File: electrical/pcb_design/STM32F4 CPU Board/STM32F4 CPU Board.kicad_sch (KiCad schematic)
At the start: 37 parts, among them J1 STLINK_STDC14, J2 STLINK_TagConnect_6, J3 Conn_01x15_Pin, J4 Conn_01x15_Pin, M1 M3, M2 M3, M3 M3, M4 M3, U1 STM32F405RGT6, U2 AMS1117-3.3, Y1 16MHz

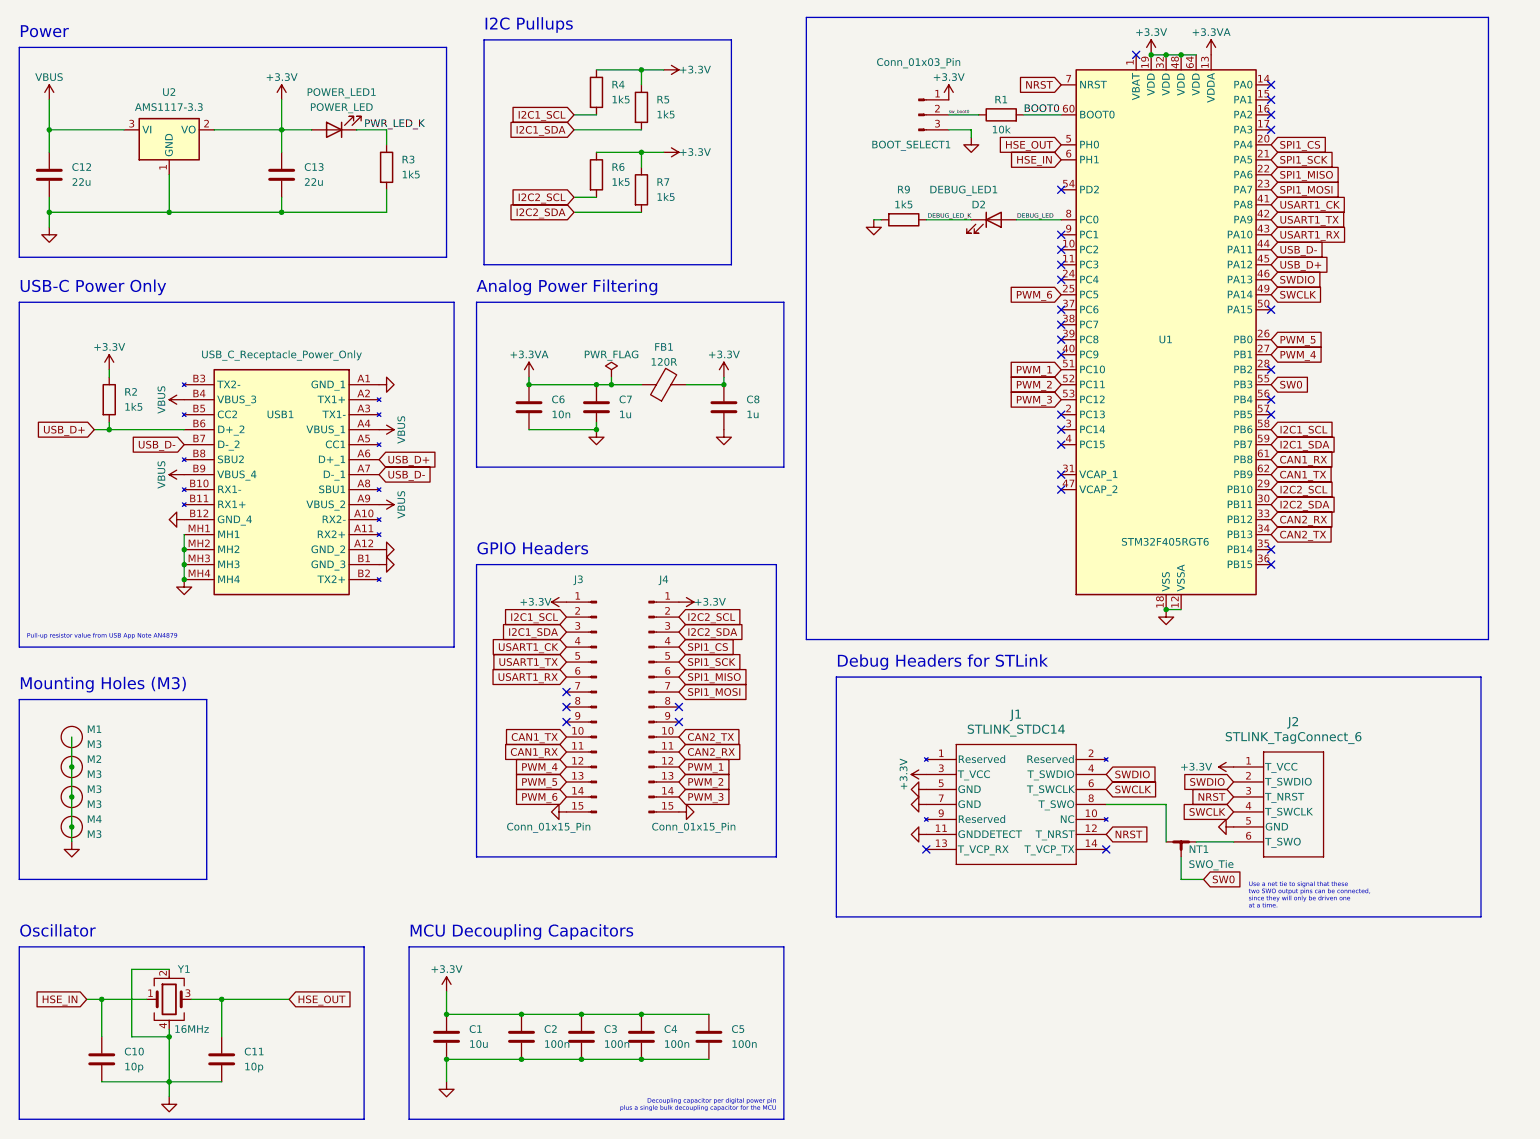
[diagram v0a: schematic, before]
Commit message: Starting layout of STM32F4 CPU board
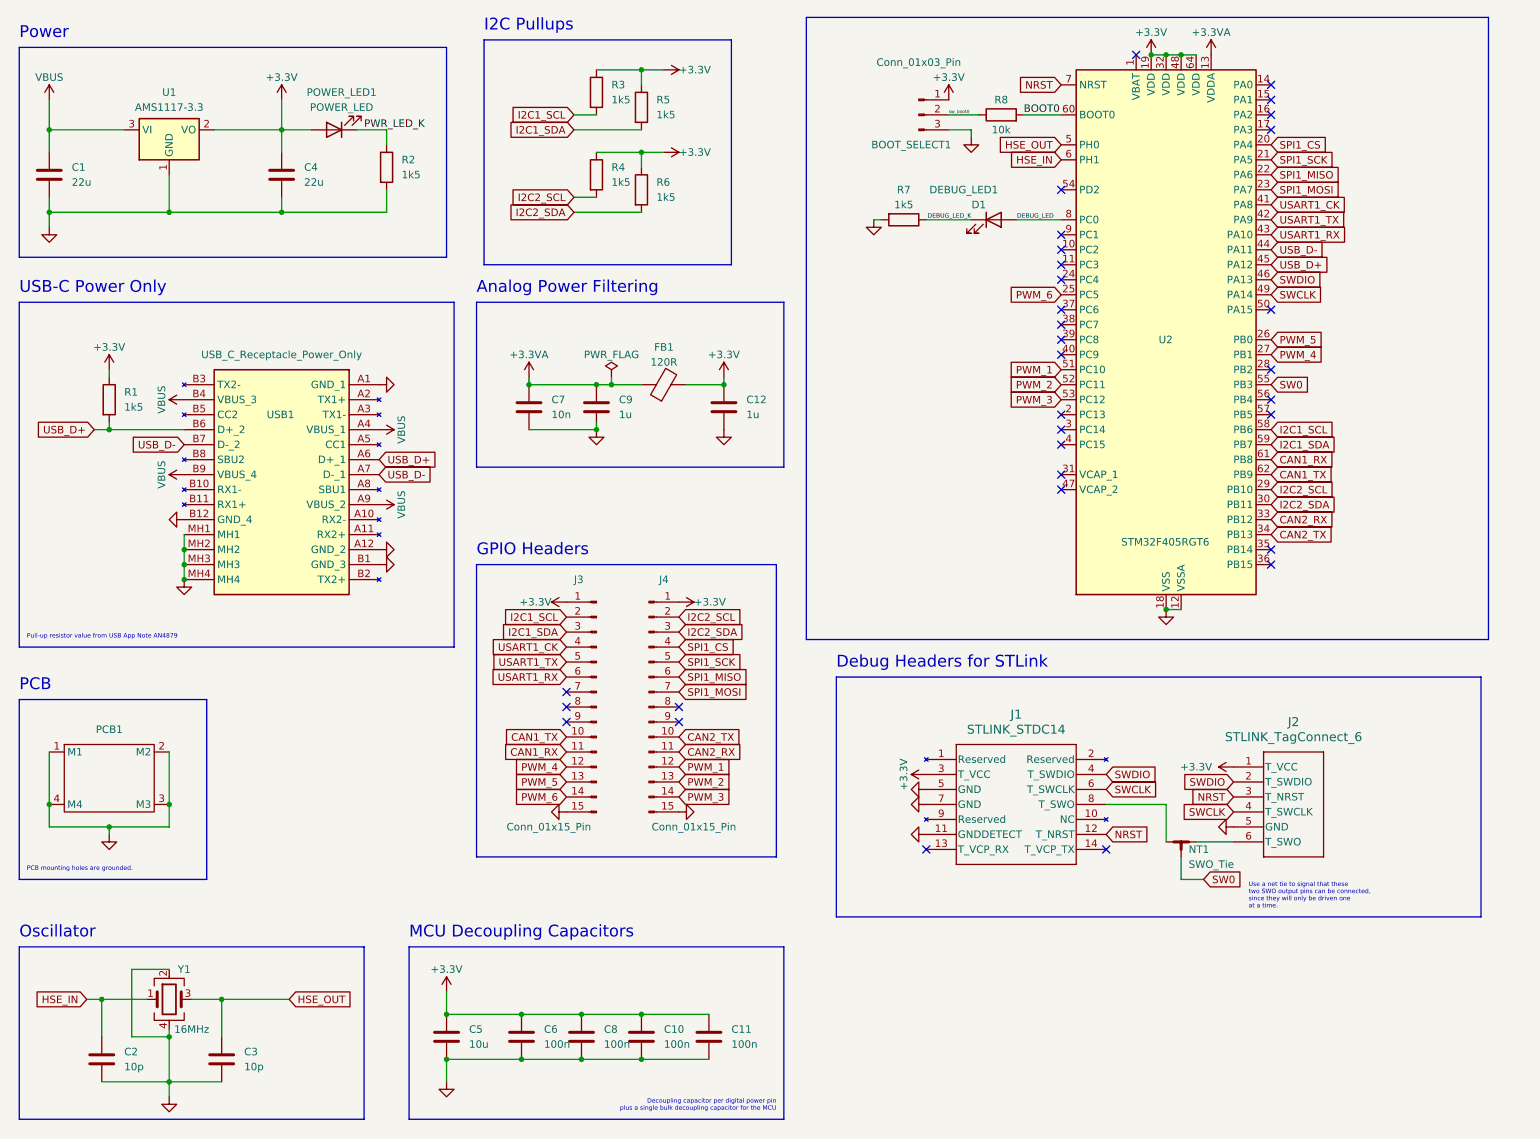
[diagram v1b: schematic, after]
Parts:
- removed M1, M2, M3, M4: M3, MountingHole:MountingHole_3.2mm_M3_ISO7380_Pad_TopBottom, symbol TVSC:Mounting_Hole_M3_ISO_7380
- added PCB1: ~, footprints:Standard_PCB_Shape, symbol TVSC:Standard_PCB
- renumbered C12 to C1, C4 to C10, C5 to C11, C8 to C12, C10 to C2, C11 to C3, C13 to C4, C1 to C5, C2 to C6, C6 to C7, C3 to C8, C7 to C9, D2 to D1, R2 to R1, R3 to R2, R4 to R3, R6 to R4, R7 to R6, R9 to R7, R1 to R8, U2 to U1, U1 to U2
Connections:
- net GND: now also PCB1.1 (M1), PCB1.2 (M2), PCB1.3 (M3), PCB1.4 (M4)
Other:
- note added: "PCB"
- note added: "PCB mounting holes are grounded."
- note removed: "Mounting Holes (M3)"

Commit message: Added CAN transceivers to CPU board
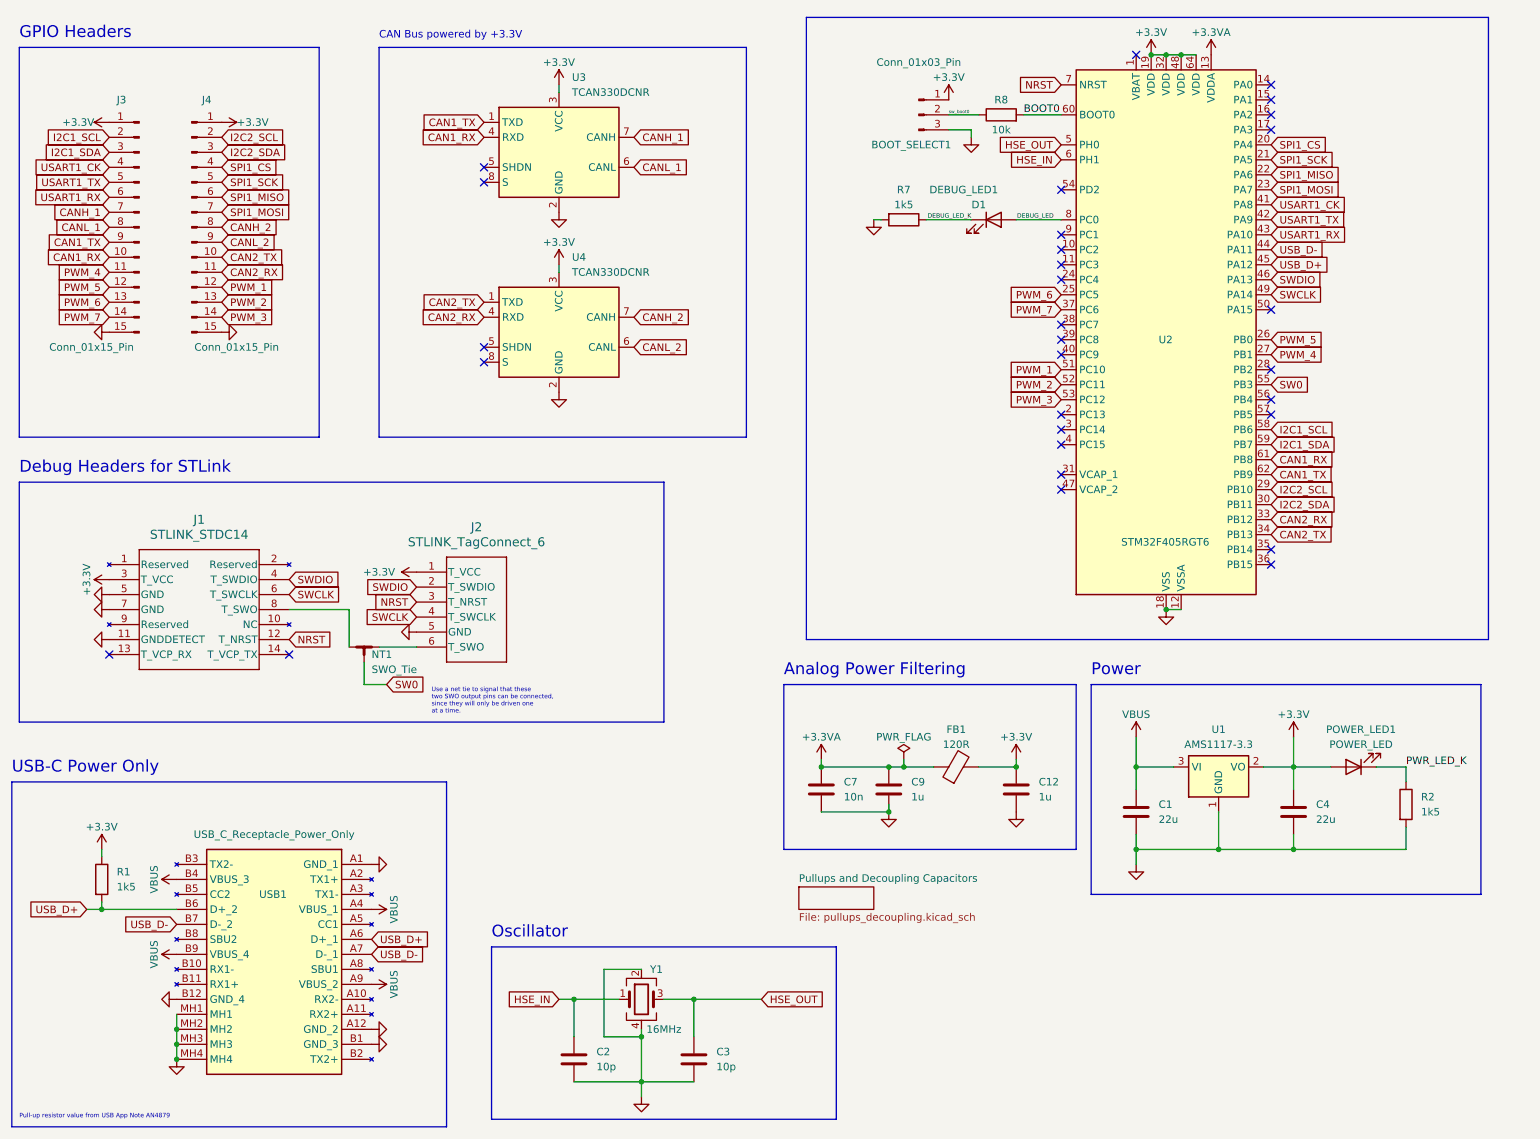
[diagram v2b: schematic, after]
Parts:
- removed C10, C11, C6, C8: 100n, Capacitor_SMD:C_0402_1005Metric, symbol Device:C
- removed C5: 10u, Capacitor_SMD:C_0603_1608Metric, symbol Device:C
- removed PCB1: ~, footprints:Standard_PCB_Shape, symbol TVSC:Standard_PCB
- removed R3, R4, R5, R6: 1k5, Resistor_SMD:R_0402_1005Metric, symbol Device:R
- added U3, U4: TCAN330DCNR, Package_TO_SOT_SMD:SOT-23-8, symbol Interface_CAN_LIN:TCAN330
- U2: MPN (none) -> C15742; Manufacturer (none) -> STMicroelectronics; Manufacturer Part Number (none) -> STM32F405RGT6
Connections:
- net +3.3V: now also U3.3 (VCC), U4.3 (VCC)
- net CAN1_RX: now also J3.10 (Pin_10), U3.4 (RXD); no longer J3.11 (Pin_11)
- net CAN1_TX: now also J3.9 (Pin_9), U3.1 (TXD); no longer J3.10 (Pin_10)
- net CAN2_RX: now also U4.4 (RXD)
- net CAN2_TX: now also U4.1 (TXD)
- net GND: now also U3.2 (GND), U4.2 (GND)
- net PWM_4: now also J3.11 (Pin_11); no longer J3.12 (Pin_12)
- net PWM_5: now also J3.12 (Pin_12); no longer J3.13 (Pin_13)
- net PWM_6: now also J3.13 (Pin_13); no longer J3.14 (Pin_14)
- net PWM_7: now reaches U2.37 (PC6)
- net PWM_7: now also J3.14 (Pin_14)
- net CANH_2: now reaches J4.8 (Pin_8)
- net CANH_2: now also U4.7 (CANH)
- net CANL_2: now reaches J4.9 (Pin_9)
- net CANL_2: now also U4.6 (CANL)
- net CANH_1: now reaches J3.7 (Pin_7)
- net CANH_1: now also U3.7 (CANH)
- net CANL_1: now reaches J3.8 (Pin_8)
- net CANL_1: now also U3.6 (CANL)
- no-connect marks 32 -> 30
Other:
- added sheet Pullups and Decoupling Capacitors (pullups_decoupling.kicad_sch)
- note added: "CAN Bus powered by +3.3V"
- note removed: "Decoupling capacitor per digital power pin plus a single bulk decoupling capacitor for the MCU"
- note removed: "I2C Pullups"
- note removed: "MCU Decoupling Capacitors"
- note removed: "PCB"
- note removed: "PCB mounting holes are grounded."
- moved on the sheet: C2, C3, J1, J2, NT1, R1, USB1, Y1

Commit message: Restructured GPIO bank usage of STM32F4. Fixed up decoupling and stabilizing capacitors in schematic.
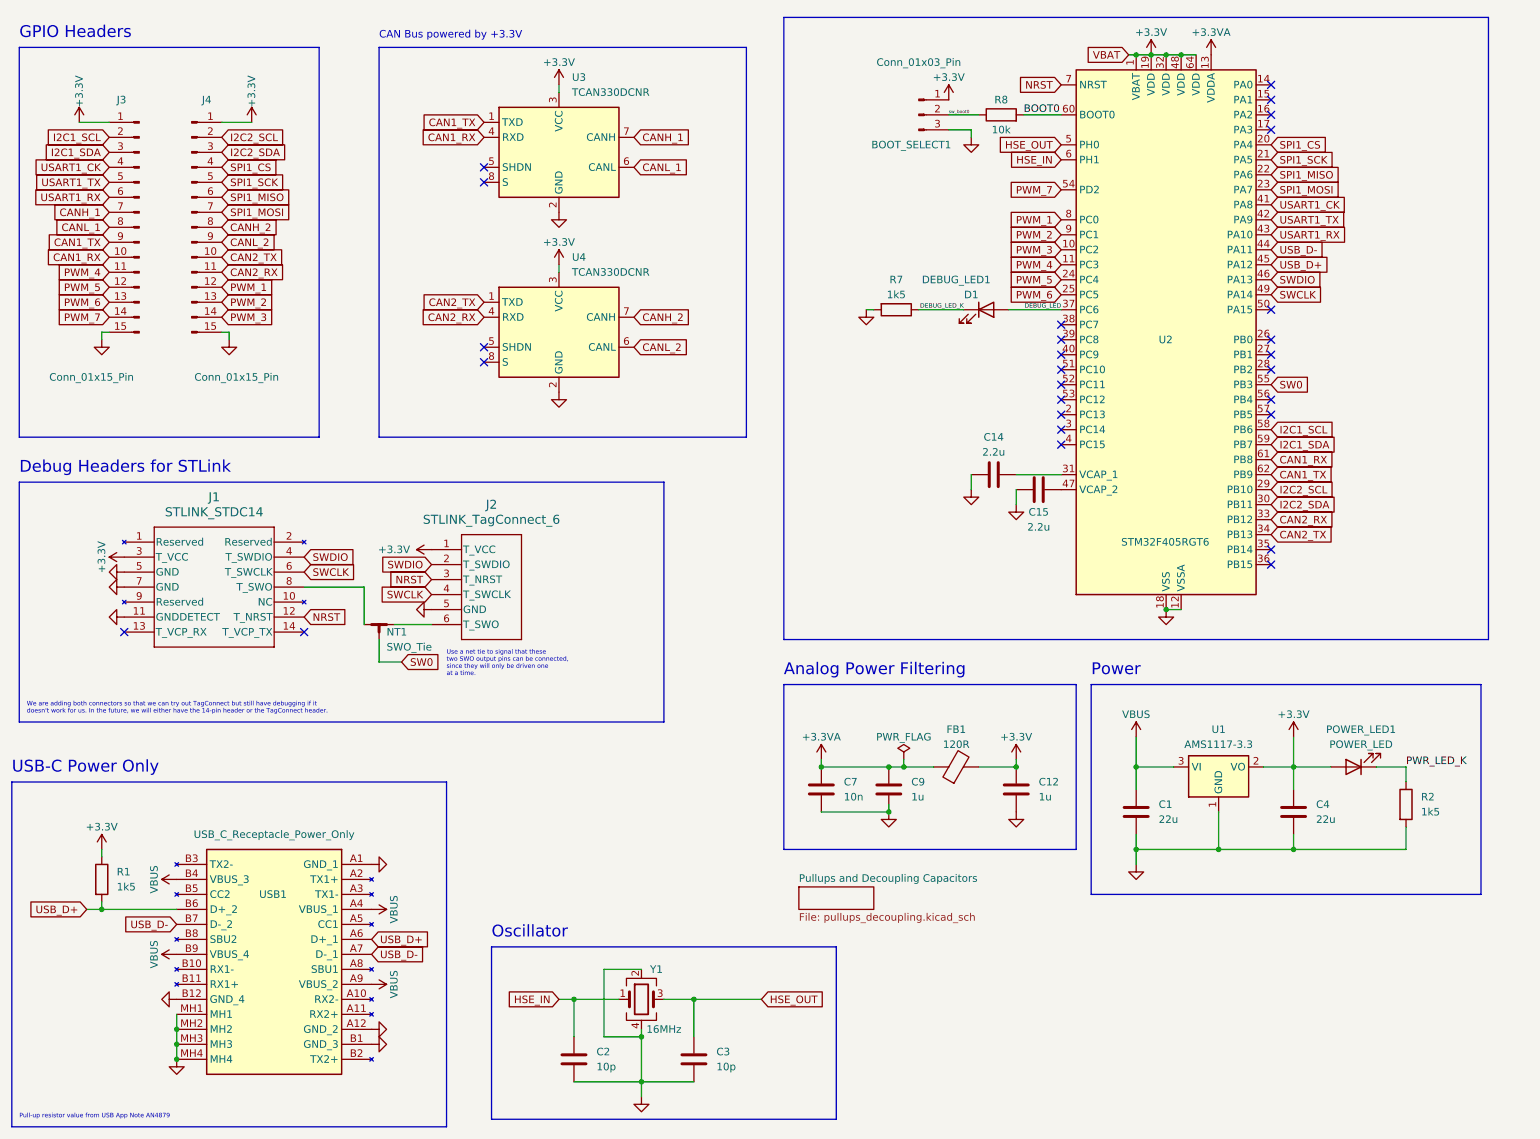
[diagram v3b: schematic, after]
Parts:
- added C14, C15: 2.2u, symbol Device:C
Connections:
- net +3.3V: now also U2.1 (VBAT)
- net DEBUG_LED: now also U2.37 (PC6); no longer U2.8 (PC0)
- net GND: now also C14.1, C15.1
- net PWM_1: now also U2.8 (PC0); no longer U2.51 (PC10)
- net PWM_2: now also U2.9 (PC1); no longer U2.52 (PC11)
- net PWM_3: now also U2.10 (PC2); no longer U2.53 (PC12)
- net PWM_4: now also U2.11 (PC3); no longer U2.27 (PB1)
- net PWM_5: now also U2.24 (PC4); no longer U2.26 (PB0)
- net PWM_7: now also U2.54 (PD2); no longer U2.37 (PC6)
- net at U2.31 (VCAP_1): now also C14.2
- net at U2.47 (VCAP_2): now also C15.2
- no-connect marks 30 -> 27
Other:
- note added: "We are adding both connectors so that we can try out TagConnect but still have debugging if it doesn't work for us. In the future, we will either have the 14-pin header or the TagConnect header."
- moved on the sheet: J1, J2, NT1

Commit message: Progress on STM32F4 board.
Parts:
- added D2: D_Schottky, Diode_SMD:D_SOD-123, symbol Device:D_Schottky
- added J5: Conn_01x02_Socket, symbol Connector:Conn_01x02_Socket
- added Q1: AO3401A, Package_TO_SOT_SMD:SOT-23, symbol Transistor_FET:AO3401A
- J2, NT1: MPN (none) -> NA
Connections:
- net GND: now also J5.2 (Pin_2), Q1.1 (G)
- net VBUS: now also D2.2 (A); no longer C1.1, U1.3 (VI)
- new net: C1.1, D2.1 (K), Q1.2 (S), U1.3 (VI)
- new net VCC: J5.1 (Pin_1), Q1.3 (D)
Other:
- moved on the sheet: C12, C2, C3, C7, C9, FB1, Y1
